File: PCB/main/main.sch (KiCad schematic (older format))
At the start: 34 parts, among them IC1 LT8316IFE#PBF, Q1 PBHV9050ZF, Q2 IXTA10P50P, Q3 SIHB24N80AE-GE3, T1 Transformer_1P_2S

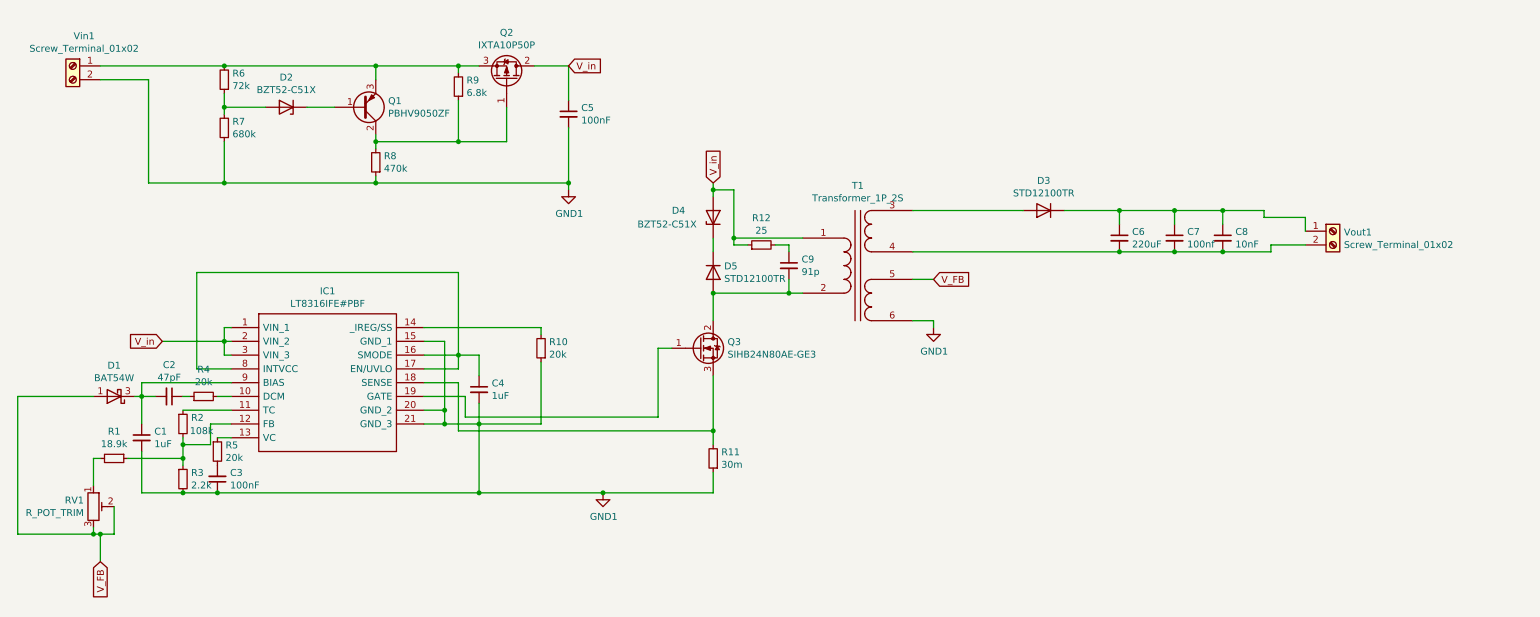
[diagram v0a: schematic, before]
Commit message: PCB updated with new mosfet&diode
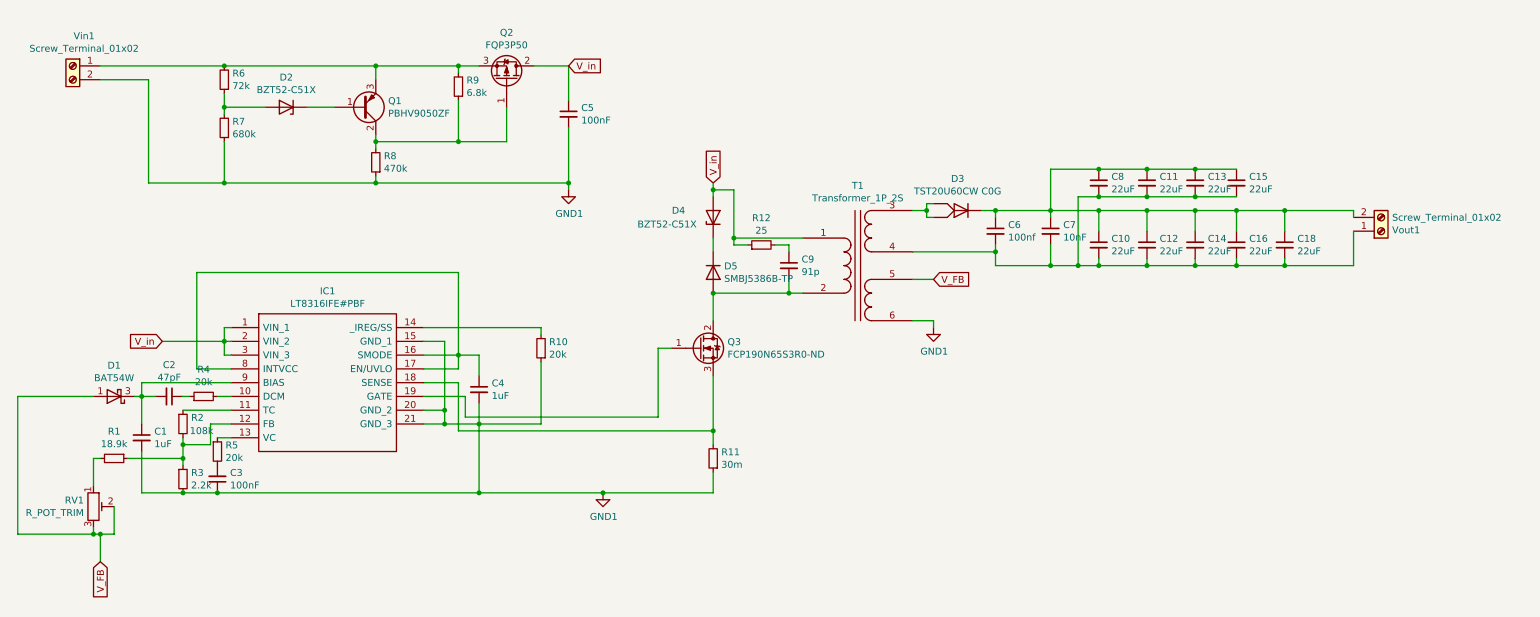
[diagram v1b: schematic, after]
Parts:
- removed C6: 220uF, Capacitor_SMD:C_Elec_8x10.2, symbol Device:C_Small
- removed D3: STD12100TR, Package_TO_SOT_SMD:TO-252-2, symbol Device:D
- added C10, C11, C12, C13, C14, C15, C16, C18, C8: 22uF, Capacitor_SMD:C_1210_3225Metric, symbol Device:C_Small
- added D3: TST20U60CW C0G, Package_TO_SOT_THT:TO-220-3_Vertical, symbol Device:D2Pak
- D5: value STD12100TR -> SMBJ5386B-TP
- Q2: value IXTA10P50P -> FQP3P50; footprint Package_TO_SOT_SMD:TO-263-2 -> Package_TO_SOT_THT:TO-220-3_Vertical
- Q3: value SIHB24N80AE-GE3 -> FCP190N65S3R0-ND; footprint Package_TO_SOT_SMD:TO-263-2 -> Package_TO_SOT_THT:TO-220-3_Vertical
- R11: footprint Resistor_SMD:R_0805_2012Metric -> Resistor_SMD:R_1218_3246Metric_Pad1.22x4.75mm_HandSolder
- renumbered C7 to C6, C8 to C7
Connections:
- net at T1.3 (SA): now also D3.1 (A), D3.3 (A)
- net at C6.2, C7.2, T1.4 (SB): now also Vout1.1 (Pin_1), C10.2, C11.2, C12.2, C13.2, C14.2, C15.2, C16.2, C18.2, C8.2; no longer Vout1.2 (Pin_2)
- net at C6.1, C7.1: now also Vout1.2 (Pin_2), C10.1, C11.1, C12.1, C13.1, C14.1, C15.1, C16.1, C18.1, C8.1, D3.2 (K); no longer Vout1.1 (Pin_1)
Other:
- moved on the sheet: C6, C7, Vout1

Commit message: script and pcb updated
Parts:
- R1: value 18.9k -> 15k
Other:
- note added: "Voltage Protection"
- moved on the sheet: Vout1
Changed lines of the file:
@@
 P 1350 3850
 F 0 "R1" V 1154 3850 50  0000 C CNN
-F 1 "18.9k" V 1245 3850 50  0000 C CNN
+F 1 "15k" V 1245 3850 50  0000 C CNN
 F 2 "Resistor_SMD:R_0805_2012Metric" H 1350 3850 50  0001 C CNN
 F 3 "~" H 1350 3850 50  0001 C CNN
@@
 L Connector:Screw_Terminal_01x02 Vout1
 U 1 1 609877F0
-P 10550 2200
-F 0 "Vout1" H 10630 2192 50  0000 L CNN
-F 1 "Screw_Terminal_01x02" H 10630 2101 50  0000 L CNN
-F 2 "TerminalBlock:TerminalBlock_Altech_AK300-2_P5.00mm" H 10550 2200 50  0001 C CNN
-F 3 "~" H 10550 2200 50  0001 C CNN
-	1    10550 2200
+P 10350 2200
+F 0 "Vout1" H 10430 2192 50  0000 L CNN
+F 1 "Screw_Terminal_01x02" H 10050 1900 50  0000 L CNN
+F 2 "TerminalBlock:TerminalBlock_Altech_AK300-2_P5.00mm" H 10350 2200 50  0001 C CNN
+F 3 "~" H 10350 2200 50  0001 C CNN
+	1    10350 2200
 	1    0    0    1
 $EndComp
@@
 	7650 2050 7750 2050
 Wire Wire Line
-	10350 2050 10350 2100
-Wire Wire Line
-	10350 2200 10350 2450
-Wire Wire Line
-	10350 2450 9850 2450
+	10150 2050 10150 2100
+Wire Wire Line
+	10150 2200 10150 2450
 Wire Wire Line
 	7750 2450 7750 2350
@@
 Wire Wire Line
 	9850 2400 9850 2450
-Connection ~ 9850 2450
-Wire Wire Line
-	9850 2450 9500 2450
 Wire Wire Line
 	8150 2050 8150 1750
@@
 Connection ~ 9500 2050
 Wire Wire Line
+	9850 2200 9850 2050
+Wire Wire Line
+	7150 2350 7750 2350
+Wire Wire Line
 	9500 2050 9850 2050
 Wire Wire Line
-	9850 2200 9850 2050
+	9500 2450 9850 2450
+Wire Wire Line
+	9850 2450 10150 2450
+Connection ~ 9850 2450
+Wire Wire Line
+	10150 2050 9850 2050
 Connection ~ 9850 2050
-Wire Wire Line
-	9850 2050 10350 2050
-Wire Wire Line
-	7150 2350 7750 2350
+Wire Notes Line
+	4500 600  1900 600
+Wire Notes Line
+	1900 600  1900 2000
+Wire Notes Line
+	1900 2000 4500 2000
+Wire Notes Line
+	4500 600  4500 2000
+Text Notes 2200 900  0    50   ~ 0
+Voltage Protection
 $EndSCHEMATC
